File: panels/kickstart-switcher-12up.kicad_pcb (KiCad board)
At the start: 2 copper layers, 88.9 x 98.4 mm, 173 parts, among them P1 CONN_01X04, Q1 Q_NMOS_GSD, U1 74HC74, U2 74HC14

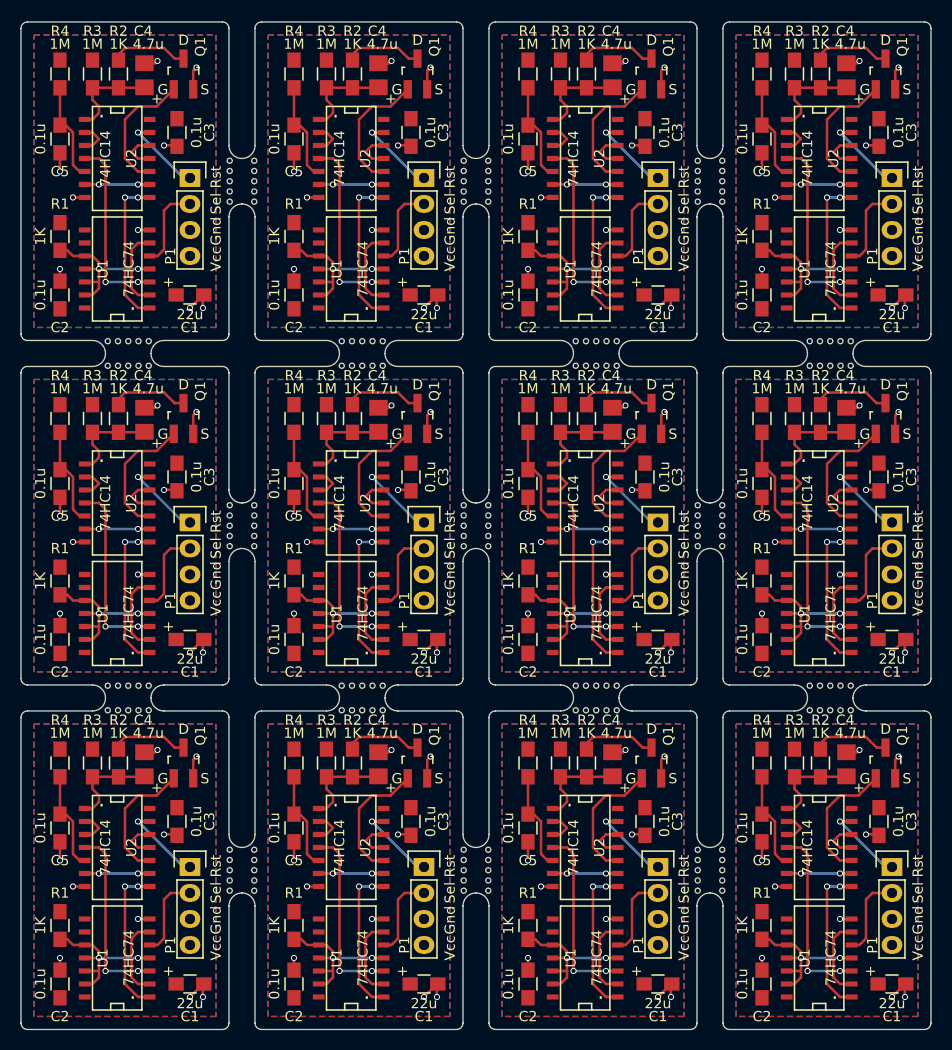
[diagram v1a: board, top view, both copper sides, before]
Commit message: kickstart-switcher: Add 1K protection resistors to RC delay HCMOS inputs. Prevents excessive current through over-voltage diodes on power down.
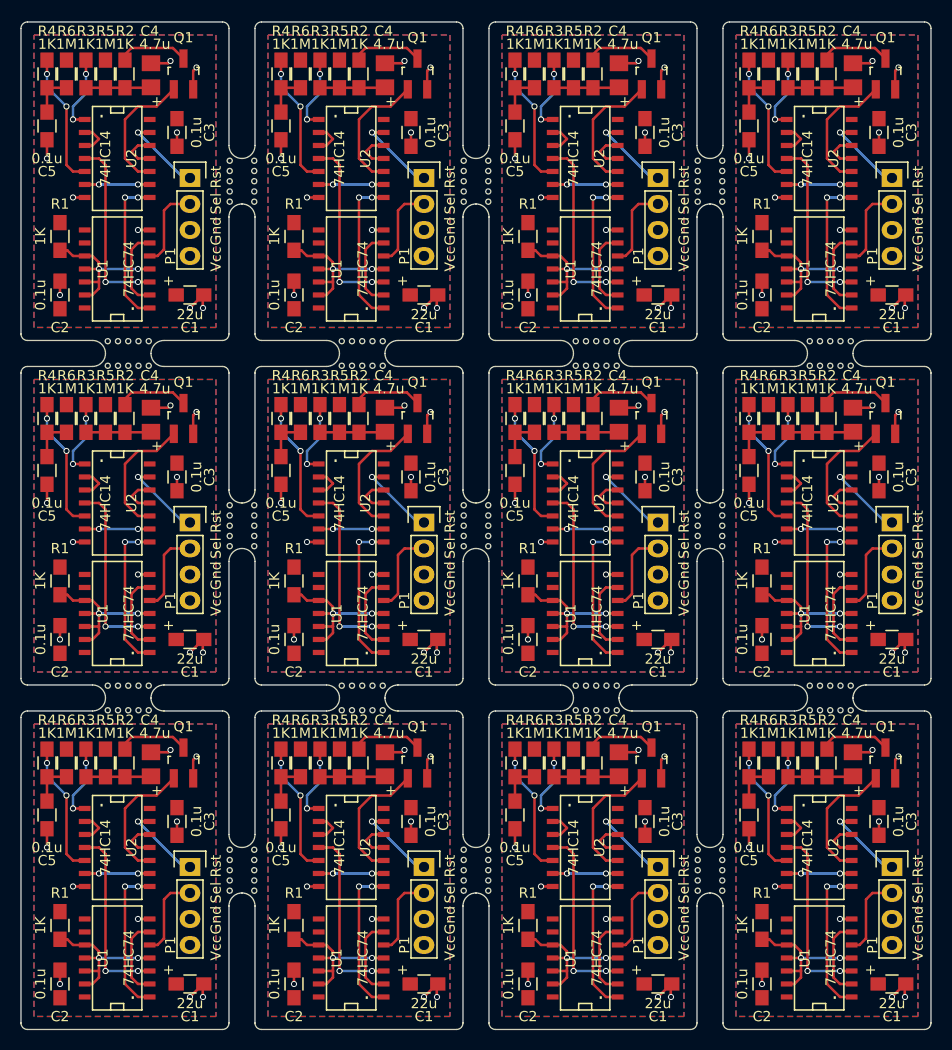
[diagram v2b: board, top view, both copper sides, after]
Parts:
- removed the C4 at (173.4, 129.7)
- removed the C4 at (104.8, 96.0)
- removed the C4 at (150.5, 96.0)
- removed the C4 at (150.5, 129.7)
- removed the C4 at (104.8, 129.7)
- removed the C4 at (127.6, 129.7)
- removed the C4 at (173.4, 62.4)
- removed the C4 at (150.5, 62.4)
- removed the C4 at (104.8, 62.4)
- removed the C4 at (127.6, 62.4)
- removed the C4 at (127.6, 96.0)
- removed the C5 at (165.1, 135.9)
- removed the C5 at (96.5, 102.2)
- removed the C5 at (142.2, 102.2)
- removed the C5 at (142.2, 135.9)
- removed the C5 at (96.5, 135.9)
- removed the C5 at (119.4, 135.9)
- removed the C5 at (165.1, 68.6)
- removed the C5 at (142.2, 68.6)
- removed the C5 at (96.5, 68.6)
- removed the C5 at (119.4, 68.6)
- removed the C5 at (119.4, 102.2)
- removed the R2 at (170.8, 129.5)
- removed the R2 at (102.2, 95.9)
- removed the R2 at (148.0, 95.9)
- removed the R2 at (148.0, 129.5)
- removed the R2 at (102.2, 129.5)
- removed the R2 at (125.1, 129.5)
- removed the R2 at (170.8, 62.2)
- removed the R2 at (148.0, 62.2)
- removed the R2 at (102.2, 62.2)
- removed the R2 at (125.1, 62.2)
- removed the R2 at (125.1, 95.9)
- removed the R3 at (168.3, 129.5)
- removed the R3 at (99.7, 95.9)
- removed the R3 at (145.4, 95.9)
- removed the R3 at (145.4, 129.5)
- removed the R3 at (99.7, 129.5)
- removed the R3 at (122.6, 129.5)
- removed the R3 at (168.3, 62.2)
- removed the R3 at (145.4, 62.2)
- removed the R3 at (99.7, 62.2)
- removed the R3 at (122.6, 62.2)
- removed the R3 at (122.6, 95.9)
- removed the R4 at (165.1, 129.5)
- removed the R4 at (96.5, 95.9)
- removed the R4 at (142.2, 95.9)
- removed the R4 at (142.2, 129.5)
- removed the R4 at (96.5, 129.5)
- removed the R4 at (119.4, 129.5)
- removed the R4 at (165.1, 62.2)
- removed the R4 at (142.2, 62.2)
- removed the R4 at (96.5, 62.2)
- removed the R4 at (119.4, 62.2)
- removed the R4 at (119.4, 95.9)
- added C4: 4.7u, FF:TantalC_SizeR_EIA-2012, F.Cu at (151.1, 129.7)
- added C4: 4.7u, FF:TantalC_SizeR_EIA-2012, F.Cu at (128.3, 62.4)
- added C4: 4.7u, FF:TantalC_SizeR_EIA-2012, F.Cu at (105.4, 62.4)
- added C4: 4.7u, FF:TantalC_SizeR_EIA-2012, F.Cu at (128.3, 129.7)
- added C4: 4.7u, FF:TantalC_SizeR_EIA-2012, F.Cu at (105.4, 129.7)
- added C4: 4.7u, FF:TantalC_SizeR_EIA-2012, F.Cu at (174.0, 96.0)
- added C4: 4.7u, FF:TantalC_SizeR_EIA-2012, F.Cu at (128.3, 96.0)
- added C4: 4.7u, FF:TantalC_SizeR_EIA-2012, F.Cu at (174.0, 62.4)
- added C4: 4.7u, FF:TantalC_SizeR_EIA-2012, F.Cu at (151.1, 62.4)
- added C4: 4.7u, FF:TantalC_SizeR_EIA-2012, F.Cu at (151.1, 96.0)
- added C4: 4.7u, FF:TantalC_SizeR_EIA-2012, F.Cu at (105.4, 96.0)
- added C5: 0.1u, Resistors_SMD:R_0805_HandSoldering, F.Cu at (141.0, 134.6)
- added C5: 0.1u, Resistors_SMD:R_0805_HandSoldering, F.Cu at (118.1, 67.3)
- added C5: 0.1u, Resistors_SMD:R_0805_HandSoldering, F.Cu at (95.2, 67.3)
- added C5: 0.1u, Resistors_SMD:R_0805_HandSoldering, F.Cu at (118.1, 134.6)
- added C5: 0.1u, Resistors_SMD:R_0805_HandSoldering, F.Cu at (95.2, 134.6)
- added C5: 0.1u, Resistors_SMD:R_0805_HandSoldering, F.Cu at (163.8, 101.0)
- added C5: 0.1u, Resistors_SMD:R_0805_HandSoldering, F.Cu at (118.1, 101.0)
- added C5: 0.1u, Resistors_SMD:R_0805_HandSoldering, F.Cu at (163.8, 67.3)
- added C5: 0.1u, Resistors_SMD:R_0805_HandSoldering, F.Cu at (141.0, 67.3)
- added C5: 0.1u, Resistors_SMD:R_0805_HandSoldering, F.Cu at (141.0, 101.0)
- added C5: 0.1u, Resistors_SMD:R_0805_HandSoldering, F.Cu at (95.2, 101.0)
- added R2: 1K, Resistors_SMD:R_0805_HandSoldering, F.Cu at (148.6, 129.5)
- added R2: 1K, Resistors_SMD:R_0805_HandSoldering, F.Cu at (125.7, 62.2)
- added R2: 1K, Resistors_SMD:R_0805_HandSoldering, F.Cu at (102.9, 62.2)
- added R2: 1K, Resistors_SMD:R_0805_HandSoldering, F.Cu at (125.7, 129.5)
- added R2: 1K, Resistors_SMD:R_0805_HandSoldering, F.Cu at (102.9, 129.5)
- added R2: 1K, Resistors_SMD:R_0805_HandSoldering, F.Cu at (171.4, 95.9)
- added R2: 1K, Resistors_SMD:R_0805_HandSoldering, F.Cu at (125.7, 95.9)
- added R2: 1K, Resistors_SMD:R_0805_HandSoldering, F.Cu at (171.4, 62.2)
- added R2: 1K, Resistors_SMD:R_0805_HandSoldering, F.Cu at (148.6, 62.2)
- added R2: 1K, Resistors_SMD:R_0805_HandSoldering, F.Cu at (148.6, 95.9)
- added R2: 1K, Resistors_SMD:R_0805_HandSoldering, F.Cu at (102.9, 95.9)
- added R3: 1K, Resistors_SMD:R_0805_HandSoldering, F.Cu at (144.8, 129.5)
- added R3: 1K, Resistors_SMD:R_0805_HandSoldering, F.Cu at (121.9, 62.2)
- added R3: 1K, Resistors_SMD:R_0805_HandSoldering, F.Cu at (99.1, 62.2)
- added R3: 1K, Resistors_SMD:R_0805_HandSoldering, F.Cu at (121.9, 129.5)
- added R3: 1K, Resistors_SMD:R_0805_HandSoldering, F.Cu at (99.1, 129.5)
- added R3: 1K, Resistors_SMD:R_0805_HandSoldering, F.Cu at (167.6, 95.9)
- added R3: 1K, Resistors_SMD:R_0805_HandSoldering, F.Cu at (121.9, 95.9)
- added R3: 1K, Resistors_SMD:R_0805_HandSoldering, F.Cu at (167.6, 62.2)
- added R3: 1K, Resistors_SMD:R_0805_HandSoldering, F.Cu at (144.8, 62.2)
- added R3: 1K, Resistors_SMD:R_0805_HandSoldering, F.Cu at (144.8, 95.9)
- added R3: 1K, Resistors_SMD:R_0805_HandSoldering, F.Cu at (99.1, 95.9)
- added R4: 1K, Resistors_SMD:R_0805_HandSoldering, F.Cu at (141.0, 129.5)
- added R4: 1K, Resistors_SMD:R_0805_HandSoldering, F.Cu at (118.1, 62.2)
- added R4: 1K, Resistors_SMD:R_0805_HandSoldering, F.Cu at (95.2, 62.2)
- added R4: 1K, Resistors_SMD:R_0805_HandSoldering, F.Cu at (118.1, 129.5)
- added R4: 1K, Resistors_SMD:R_0805_HandSoldering, F.Cu at (95.2, 129.5)
- added R4: 1K, Resistors_SMD:R_0805_HandSoldering, F.Cu at (163.8, 95.9)
- added R4: 1K, Resistors_SMD:R_0805_HandSoldering, F.Cu at (118.1, 95.9)
- added R4: 1K, Resistors_SMD:R_0805_HandSoldering, F.Cu at (163.8, 62.2)
- added R4: 1K, Resistors_SMD:R_0805_HandSoldering, F.Cu at (141.0, 62.2)
- added R4: 1K, Resistors_SMD:R_0805_HandSoldering, F.Cu at (141.0, 95.9)
- added R4: 1K, Resistors_SMD:R_0805_HandSoldering, F.Cu at (95.2, 95.9)
- added R5: 1M, Resistors_SMD:R_0805_HandSoldering, F.Cu at (146.7, 129.5)
- added R5: 1M, Resistors_SMD:R_0805_HandSoldering, F.Cu at (123.8, 62.2)
- added R5: 1M, Resistors_SMD:R_0805_HandSoldering, F.Cu at (101.0, 62.2)
- added R5: 1M, Resistors_SMD:R_0805_HandSoldering, F.Cu at (169.5, 129.5)
- added R5: 1M, Resistors_SMD:R_0805_HandSoldering, F.Cu at (123.8, 129.5)
- added R5: 1M, Resistors_SMD:R_0805_HandSoldering, F.Cu at (101.0, 129.5)
- added R5: 1M, Resistors_SMD:R_0805_HandSoldering, F.Cu at (169.5, 95.9)
- added R5: 1M, Resistors_SMD:R_0805_HandSoldering, F.Cu at (123.8, 95.9)
- added R5: 1M, Resistors_SMD:R_0805_HandSoldering, F.Cu at (169.5, 62.2)
- added R5: 1M, Resistors_SMD:R_0805_HandSoldering, F.Cu at (146.7, 62.2)
- added R5: 1M, Resistors_SMD:R_0805_HandSoldering, F.Cu at (146.7, 95.9)
- added R5: 1M, Resistors_SMD:R_0805_HandSoldering, F.Cu at (101.0, 95.9)
- added R6: 1M, Resistors_SMD:R_0805_HandSoldering, F.Cu at (142.9, 129.5)
- added R6: 1M, Resistors_SMD:R_0805_HandSoldering, F.Cu at (120.0, 62.2)
- added R6: 1M, Resistors_SMD:R_0805_HandSoldering, F.Cu at (97.2, 62.2)
- added R6: 1M, Resistors_SMD:R_0805_HandSoldering, F.Cu at (165.7, 129.5)
- added R6: 1M, Resistors_SMD:R_0805_HandSoldering, F.Cu at (120.0, 129.5)
- added R6: 1M, Resistors_SMD:R_0805_HandSoldering, F.Cu at (97.2, 129.5)
- added R6: 1M, Resistors_SMD:R_0805_HandSoldering, F.Cu at (165.7, 95.9)
- added R6: 1M, Resistors_SMD:R_0805_HandSoldering, F.Cu at (120.0, 95.9)
- added R6: 1M, Resistors_SMD:R_0805_HandSoldering, F.Cu at (165.7, 62.2)
- added R6: 1M, Resistors_SMD:R_0805_HandSoldering, F.Cu at (142.9, 62.2)
- added R6: 1M, Resistors_SMD:R_0805_HandSoldering, F.Cu at (142.9, 95.9)
- added R6: 1M, Resistors_SMD:R_0805_HandSoldering, F.Cu at (97.2, 95.9)
- Q1 (x12): value Q_NMOS_GSD -> Q_NMOS
- R3, R4: value 1M -> 1K
- moved R4 33.7 mm to (163.8, 129.5)
- moved C4 33.7 mm to (174.0, 129.7)
- moved R2 33.7 mm to (171.4, 129.5)
- moved R3 33.7 mm to (167.6, 129.5)
- moved C1 33.7 mm to (177.8, 151.1)
- moved C1 33.7 mm to (177.8, 117.5)
- moved C2 33.7 mm to (165.1, 151.1)
- moved C2 33.7 mm to (165.1, 117.5)
- moved C3 33.7 mm to (176.5, 135.3)
- moved C3 33.7 mm to (176.5, 101.6)
- moved U1 33.7 mm to (170.6, 148.6)
- moved U1 33.7 mm to (170.6, 114.9)
- moved P1 33.7 mm to (177.8, 139.7)
- moved P1 33.7 mm to (177.8, 106.0)
- moved Q1 33.7 mm to (177.2, 129.5)
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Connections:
- R3 pad 1: VCC -> Net-(R3-Pad1)
- R4 pad 1: VCC -> Net-(R4-Pad1)
- U2 pad 1: Net-(C4-Pad1) -> Net-(R3-Pad1) (x12)
- U2 pad 5: Net-(C5-Pad1) -> Net-(R4-Pad1) (x12)
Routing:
- net Net-(R4-Pad1): track 0.00 -> 162.9 mm, vias 0 -> 24
- net Net-(R3-Pad1): track 0.00 -> 89.6 mm, vias 0 -> 24
- net Net-(C5-Pad1): track 118.3 -> 51.4 mm
- net Net-(C4-Pad1): track 117.4 -> 81.5 mm
- net GND: track 161.7 -> 170.9 mm
- net Net-(Q1-Pad3): track 91.2 -> 83.6 mm
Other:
- board text removed: "D"
- board text removed: "G"
- board text removed: "S"
